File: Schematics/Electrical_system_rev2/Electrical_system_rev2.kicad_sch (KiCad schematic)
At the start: 41 parts, among them J1 DTM04-12PA-L012, J10 DTM06-12SA, J12 DTM06-12SA, J13 DTM04-12PA-L012, J14 DTM06-12SA, J17 206429-1, J18 DTM06-12SA, J19 UPCP012ALS2, J2 DTM06-12SA, J20 211102-1, J21 DTM04-12PA-L012, J22 UPCR012ALS1, J23 33482-4001, J24 206429-1, J25 211102-1, J7 DTM04-12PA-L012, J7 UPCR012ALS1, J8 211102-1, J8 UPCP012ALS2, J9 206429-1, SW1 2843011, SW2 2843011, SW3 2843011, SW4 84-5330.0020, SW5 84-5330.0020

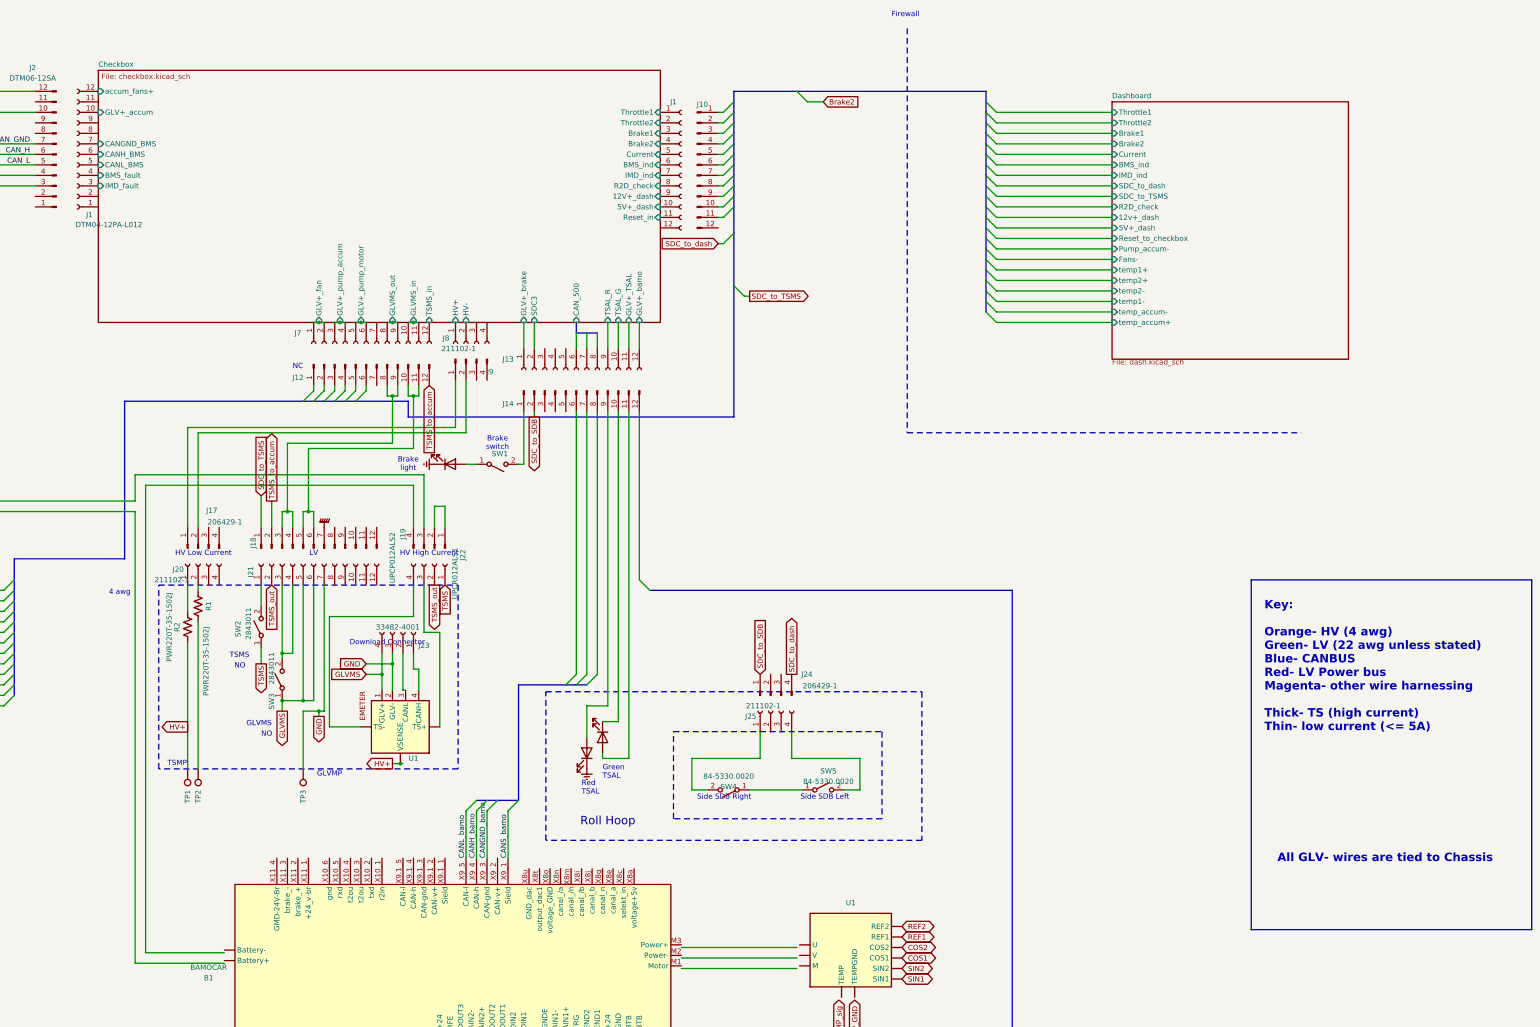
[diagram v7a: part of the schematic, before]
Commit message: moved stuff back into Checkbox :P
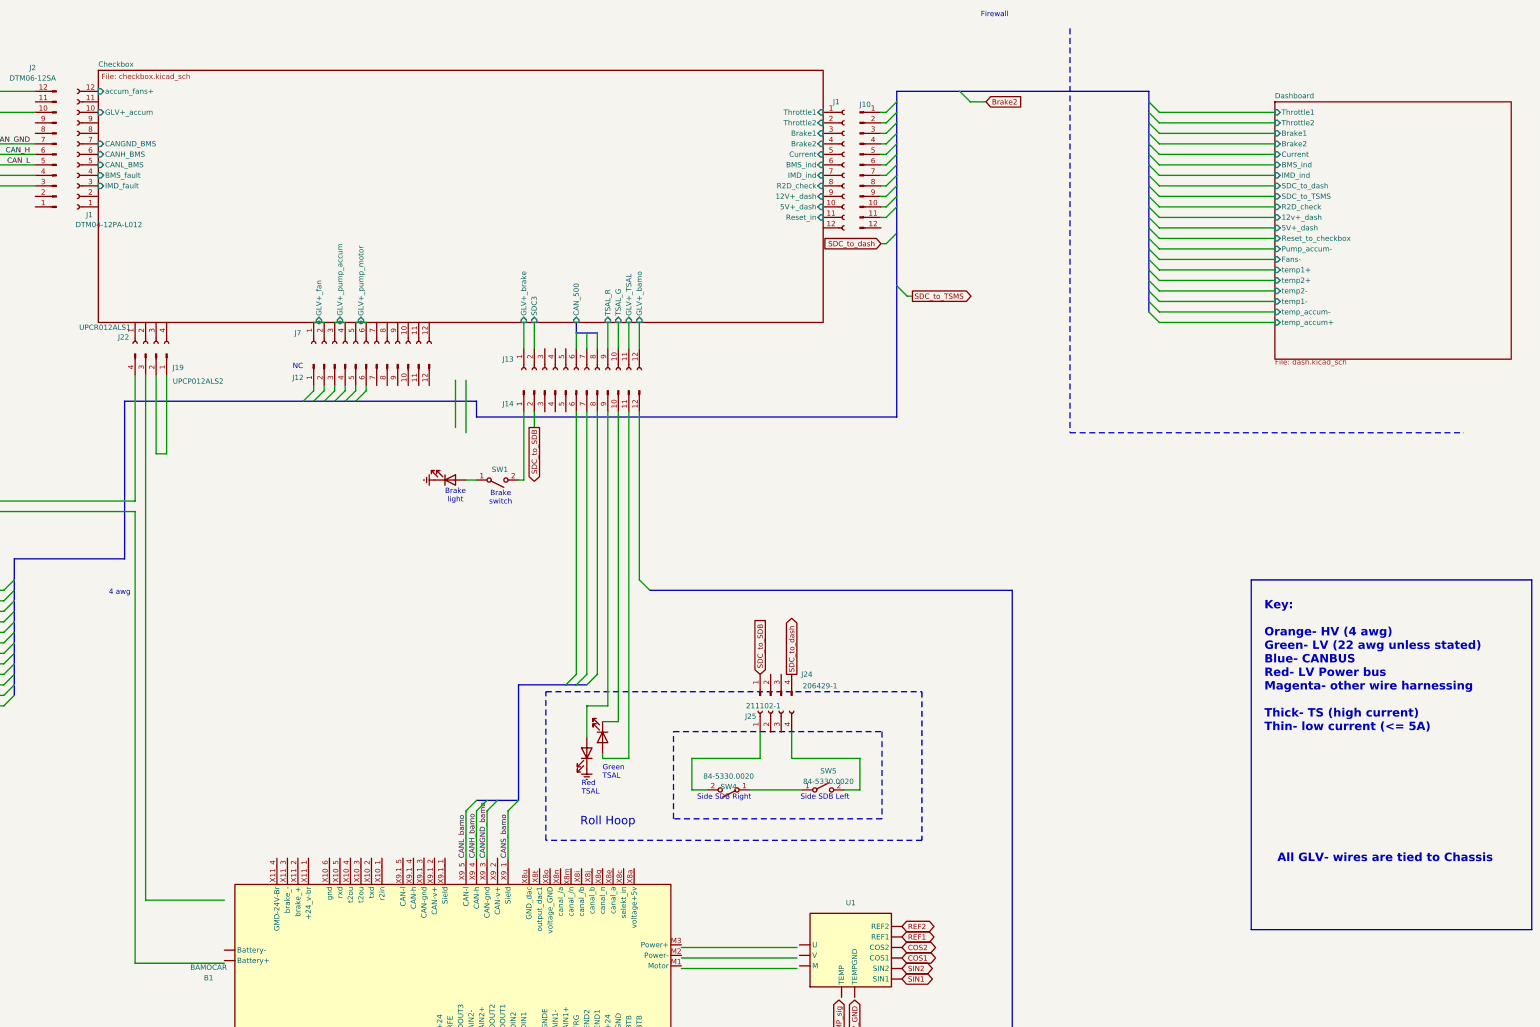
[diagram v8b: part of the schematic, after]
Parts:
- removed J17, J9: 206429-1, symbol Connector:Conn_01x04_Pin
- removed J18: DTM06-12SA, symbol Connector:Conn_01x12_Pin
- removed J20, J8: 211102-1, symbol Connector:Conn_01x04_Socket
- removed J21: DTM04-12PA-L012, symbol Connector:Conn_01x12_Socket
- removed J23: 33482-4001, symbol Connector:Conn_01x04_Socket
- removed R1, R2: PWR220T-35-1502J, symbol Device:R_US
- removed SW2, SW3: 2843011, symbol Switch:SW_SPST
- removed TP1, TP2, TP3: TestPoint, symbol Connector:TestPoint
- removed U1: ~, symbol FSAE:Emeter
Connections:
- net TSMS_to_accum: no longer J12.12 (Pin_12)
- net at J8.4 (Pin_4): now also J19.4 (Pin_4); no longer J19.3 (Pin_3)
- net at J12.8 (Pin_8): no longer J12.9 (Pin_9)
- net at J12.10 (Pin_10): no longer J12.11 (Pin_11)
- net Checkbox/GLVMS_in: no longer names the net of J7.10 (Pin_10)
- net Checkbox/GLVMS_in: no longer J7.11 (Pin_11)
- net Checkbox/GLVMS_out: no longer names the net of J7.8 (Pin_8)
- net Checkbox/GLVMS_out: no longer J7.9 (Pin_9)
- net Checkbox/TSMS_in: no longer names the net of J7.12 (Pin_12)
- net TSMS: no longer names the net of J22.1 (Pin_1)
- net TSMS_out: no longer names the net of J22.2 (Pin_2)
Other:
- sheet Checkbox ports: added none; removed GLVMS_in, GLVMS_out, HV+, HV-, TSMS_in
- note removed: "Download Connector"
- note removed: "GLVMP"
- note removed: "GLVMS"
- note removed: "HV High Current"
- note removed: "HV Low Current"
- note removed: "LV"
- note removed: "NO"
- note removed: "TSMP"
- note removed: "TSMS"
- moved on the sheet: J1, J10, J19, SW1
